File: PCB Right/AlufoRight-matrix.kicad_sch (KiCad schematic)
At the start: 62 parts, among them K11 PG1350, K12 PG1350, K13 PG1350, K14 PG1350, K15 PG1350, K16 PG1350, K21 PG1350, K22 PG1350, K23 PG1350, K24 PG1350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

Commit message: Rename righthand PCB project internally
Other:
- title: Alufo  -> Alufo

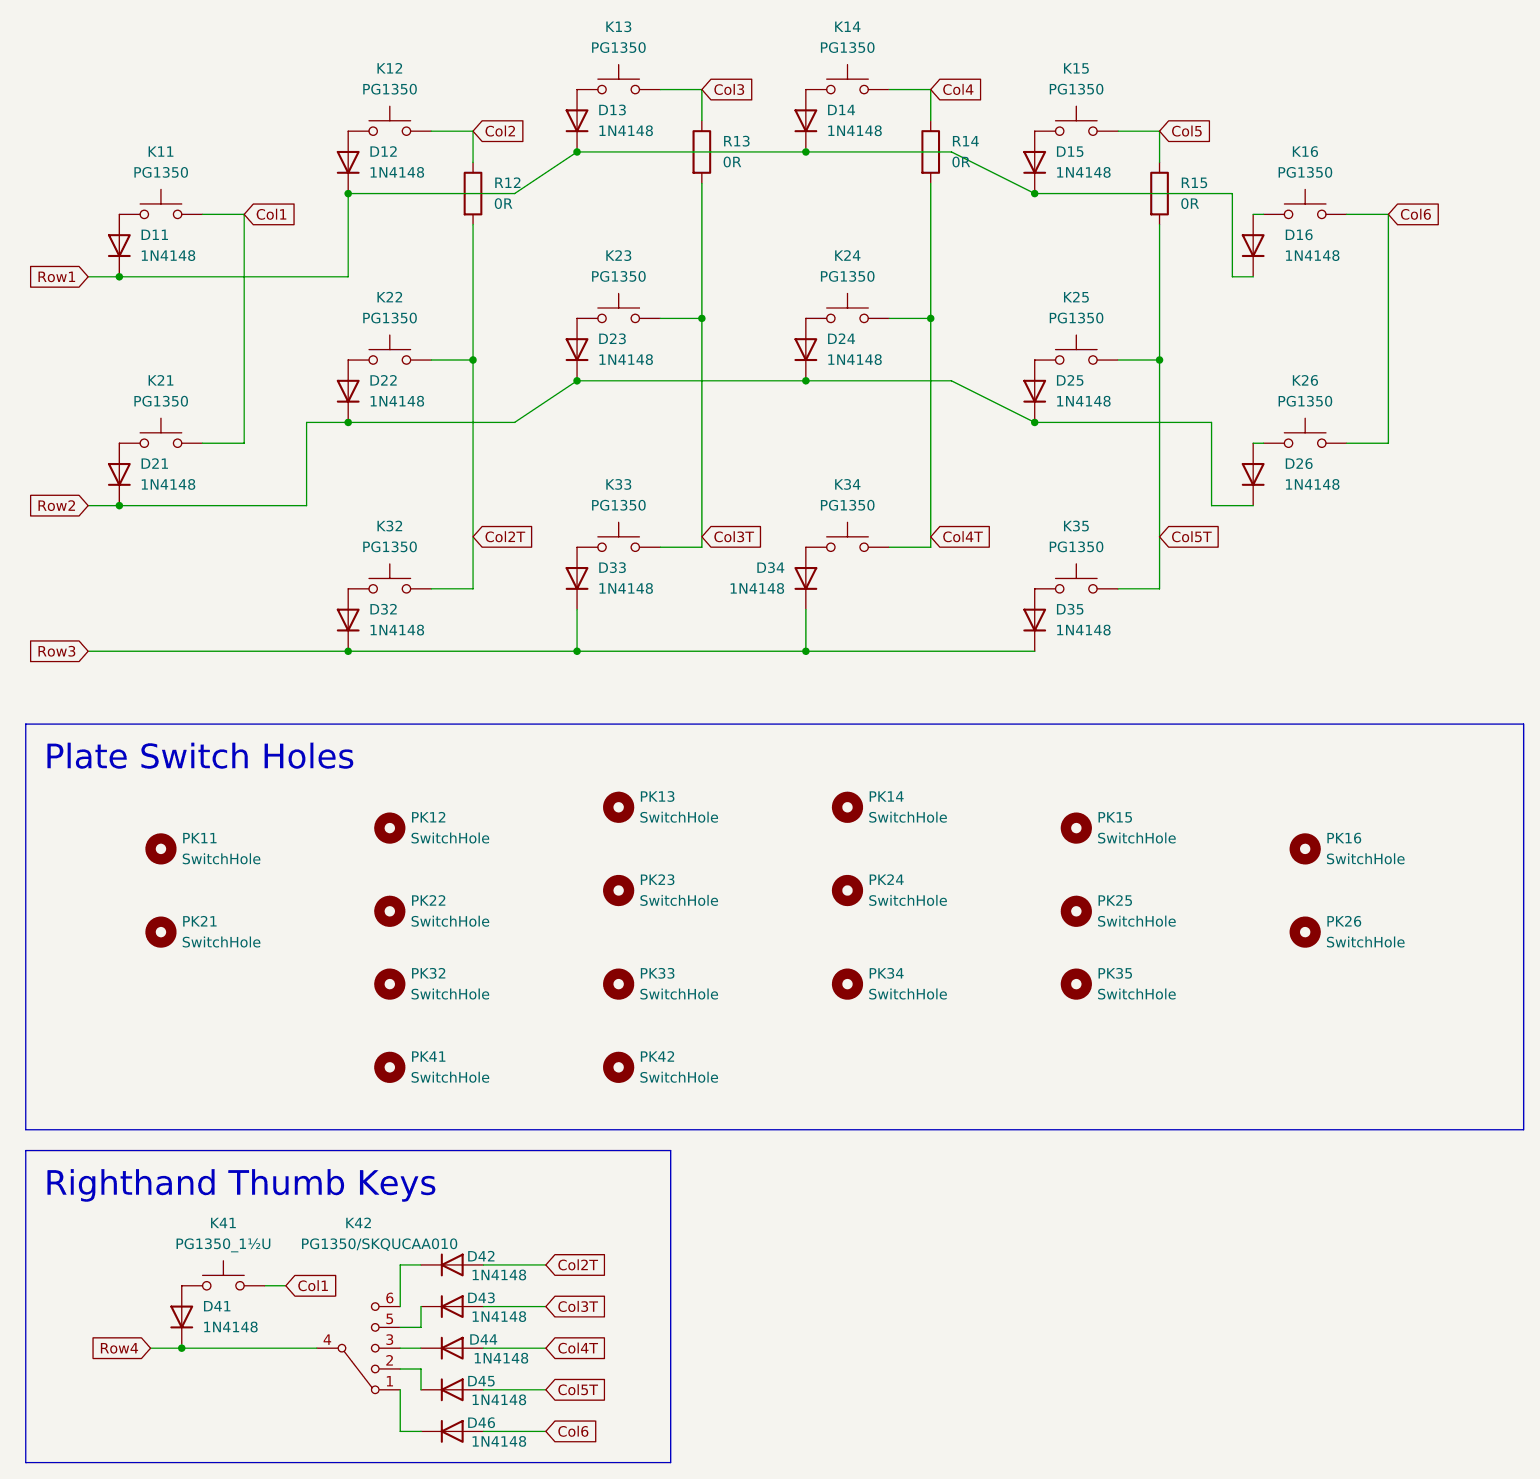
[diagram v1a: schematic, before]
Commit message: Remove plate from left and right PCBs
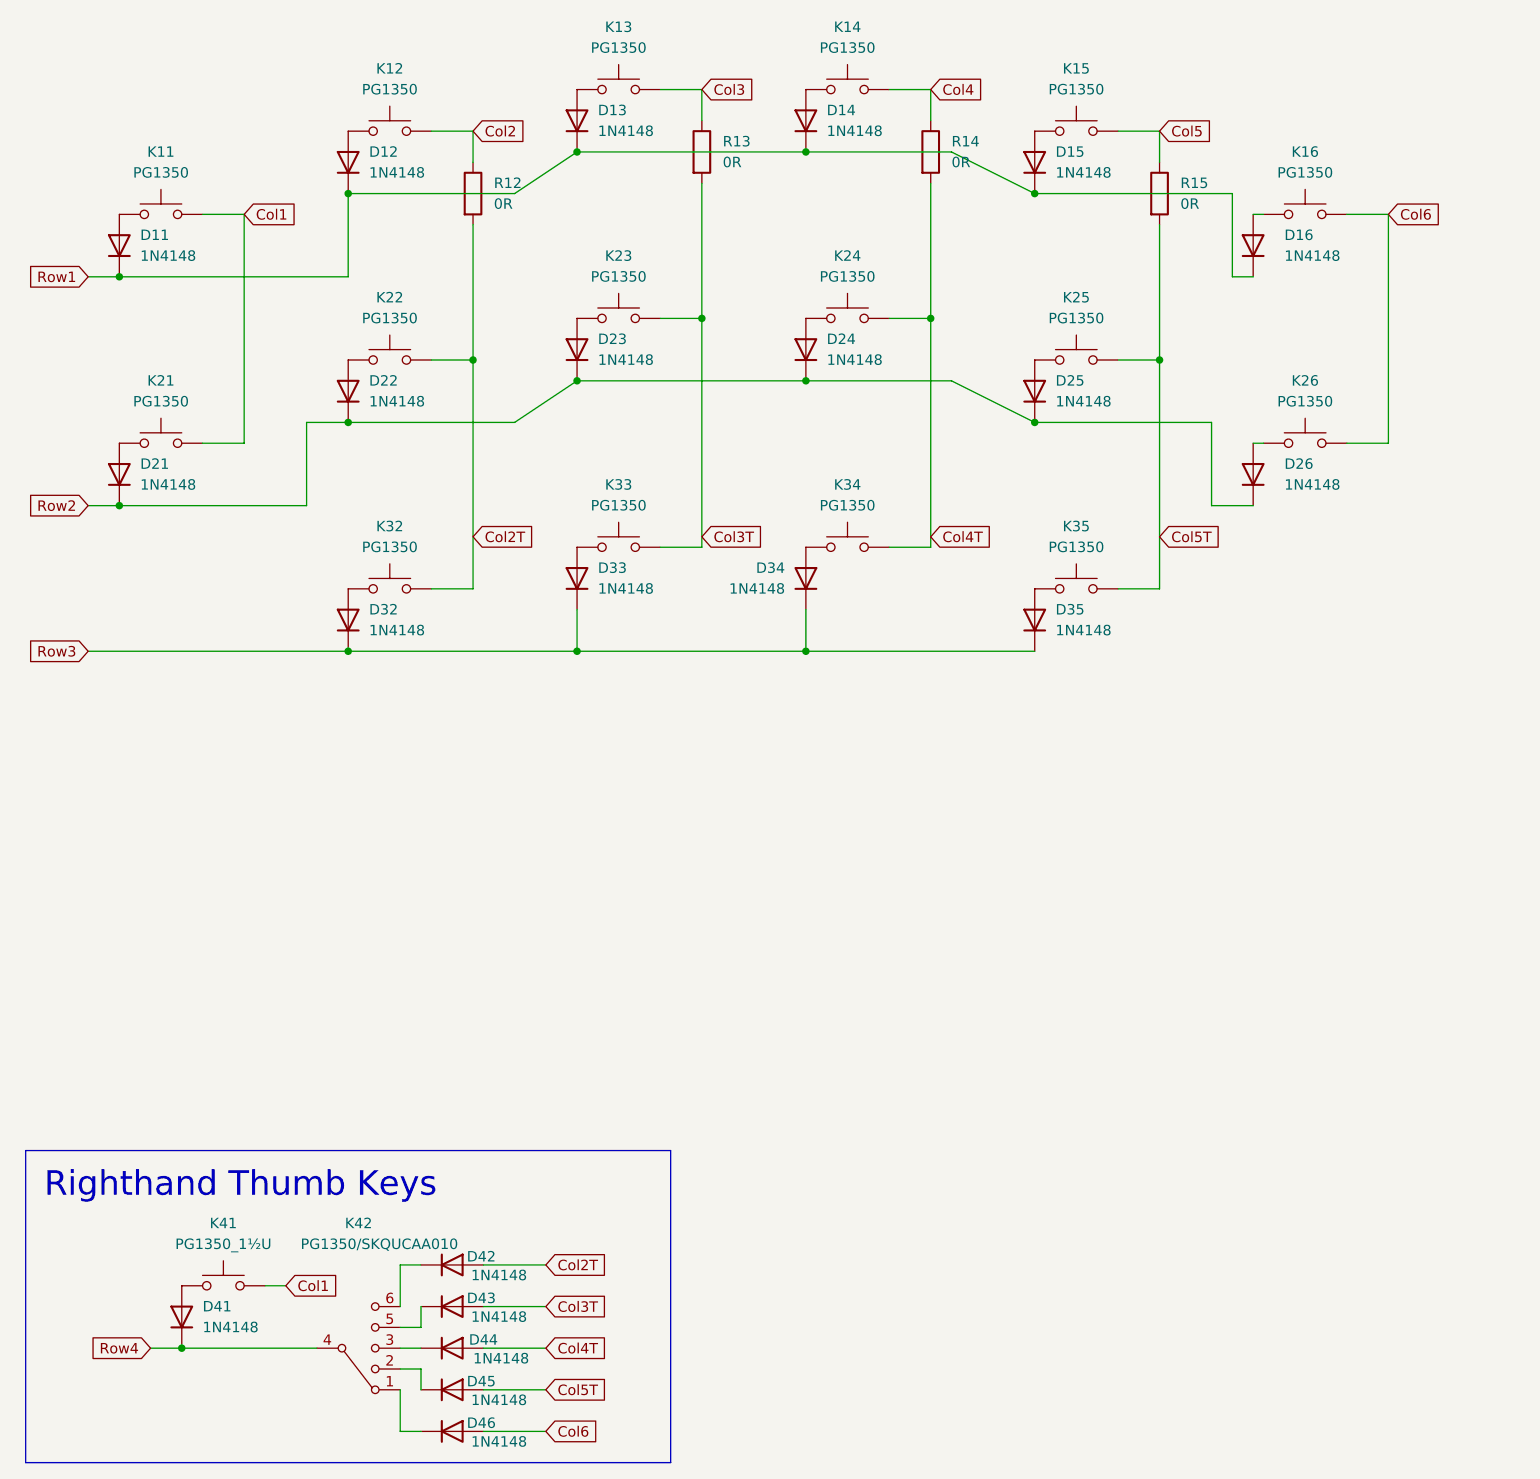
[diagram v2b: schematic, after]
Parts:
- removed PK11, PK12, PK13, PK14, PK15, PK16, PK21, PK22, PK23, PK24, PK25, PK26, PK32, PK33, PK34, PK35, PK42: SwitchHole, Project_Library:SW_choc_v1_Plate_CPG135001S30_1u, symbol Mechanical:MountingHole
- removed PK41: SwitchHole, Project_Library:SW_choc_v1_Plate_CPG135001S30_1.5u, symbol Mechanical:MountingHole
